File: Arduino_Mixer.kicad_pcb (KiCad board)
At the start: 2 copper layers, 142.5 x 99.3 mm, 7 parts

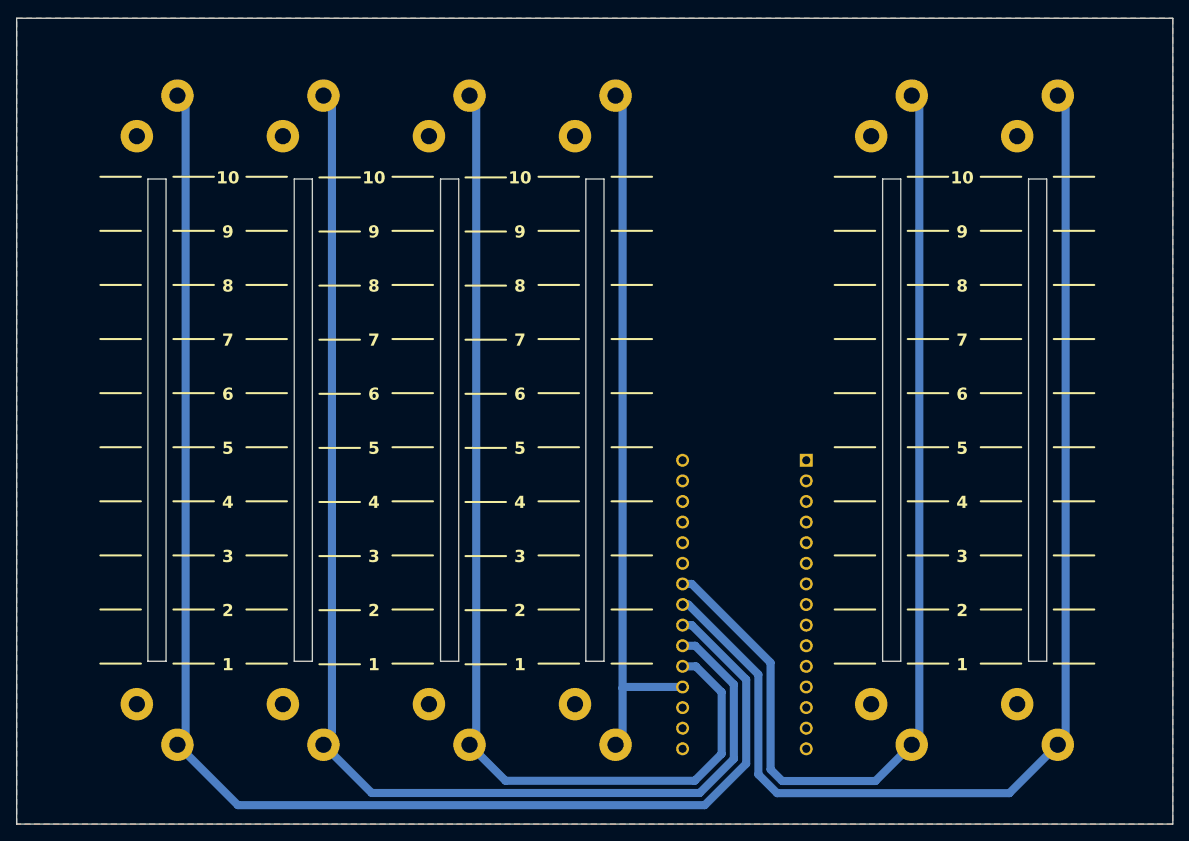
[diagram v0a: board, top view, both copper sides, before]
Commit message: Added 4 corner and 1 mid mounting hole for PCB. Generated 3D model output to use when creating 3D printed spacer (using Freecad and KiCadStepUp plugin)
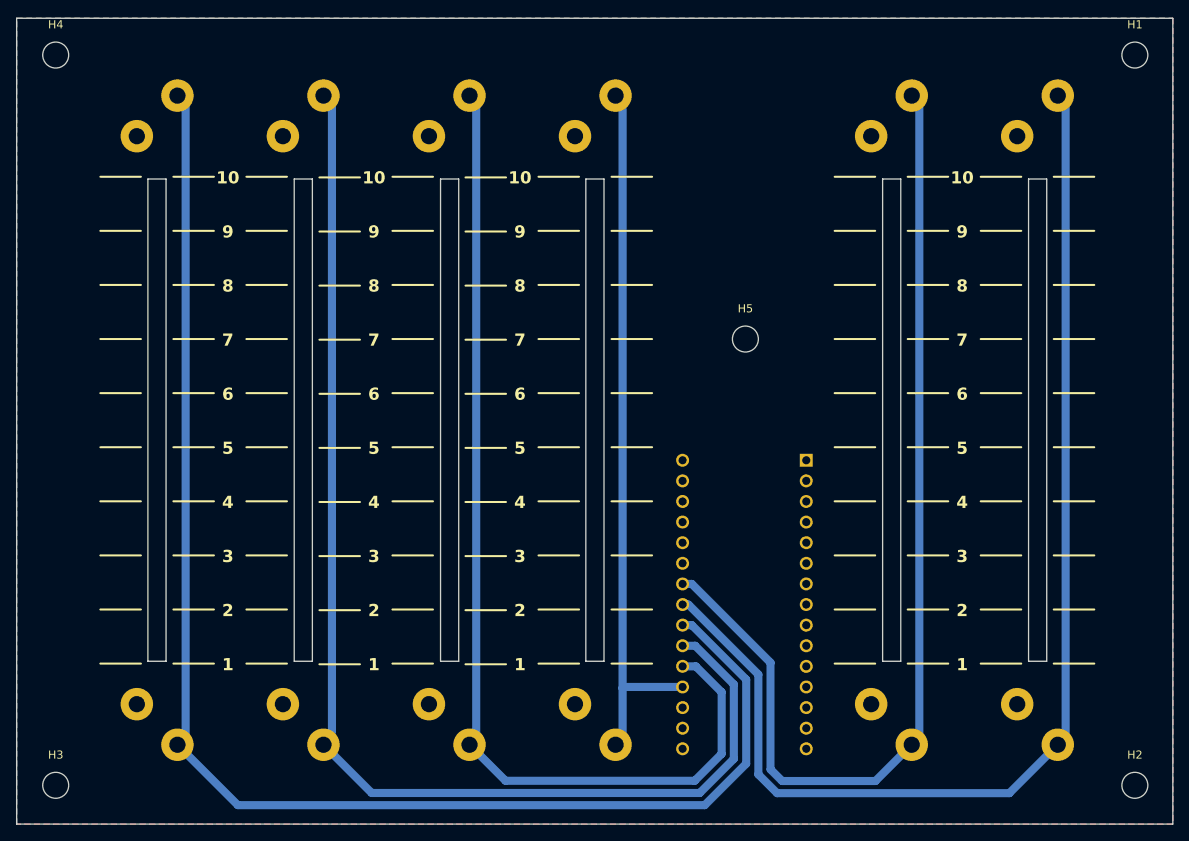
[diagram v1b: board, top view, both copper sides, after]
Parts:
- added H1: MountingHole, MountingHole:MountingHole_3.2mm_M3_ISO14580, F.Cu at (213.0, 50.0)
- added H2: MountingHole, MountingHole:MountingHole_3.2mm_M3_ISO14580, F.Cu at (213.0, 140.0)
- added H3: MountingHole, MountingHole:MountingHole_3.2mm_M3_ISO14580, F.Cu at (80.0, 140.0)
- added H4: MountingHole, MountingHole:MountingHole_3.2mm_M3_ISO14580, F.Cu at (80.0, 50.0)
- added H5: MountingHole, MountingHole:MountingHole_3.2mm_M3_ISO14580, F.Cu at (165.0, 85.0)
